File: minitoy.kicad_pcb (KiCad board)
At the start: 2 copper layers, 44 x 40 mm, 37 parts, among them J1 Conn_01x06, J2 PMOD1, J4 USB_B_Micro, J5 PMOD2, U1 ICE40UP5K-SG48, U2 ESP-12E, U3 MIC5504-3.3YM5, U4 MIC5504-1.2YM5, U5 MIC5504-3.3YM5

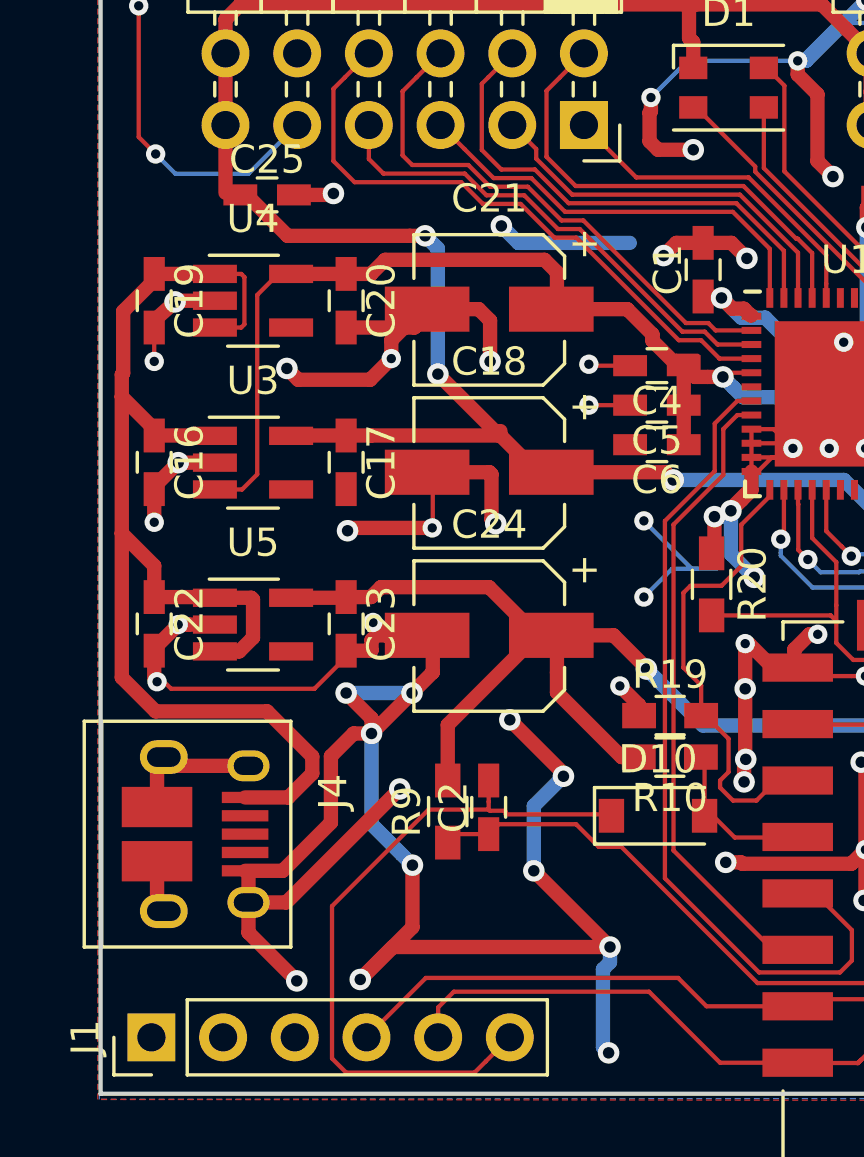
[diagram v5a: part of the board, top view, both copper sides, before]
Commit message: Fix 3d models, change USB footprint
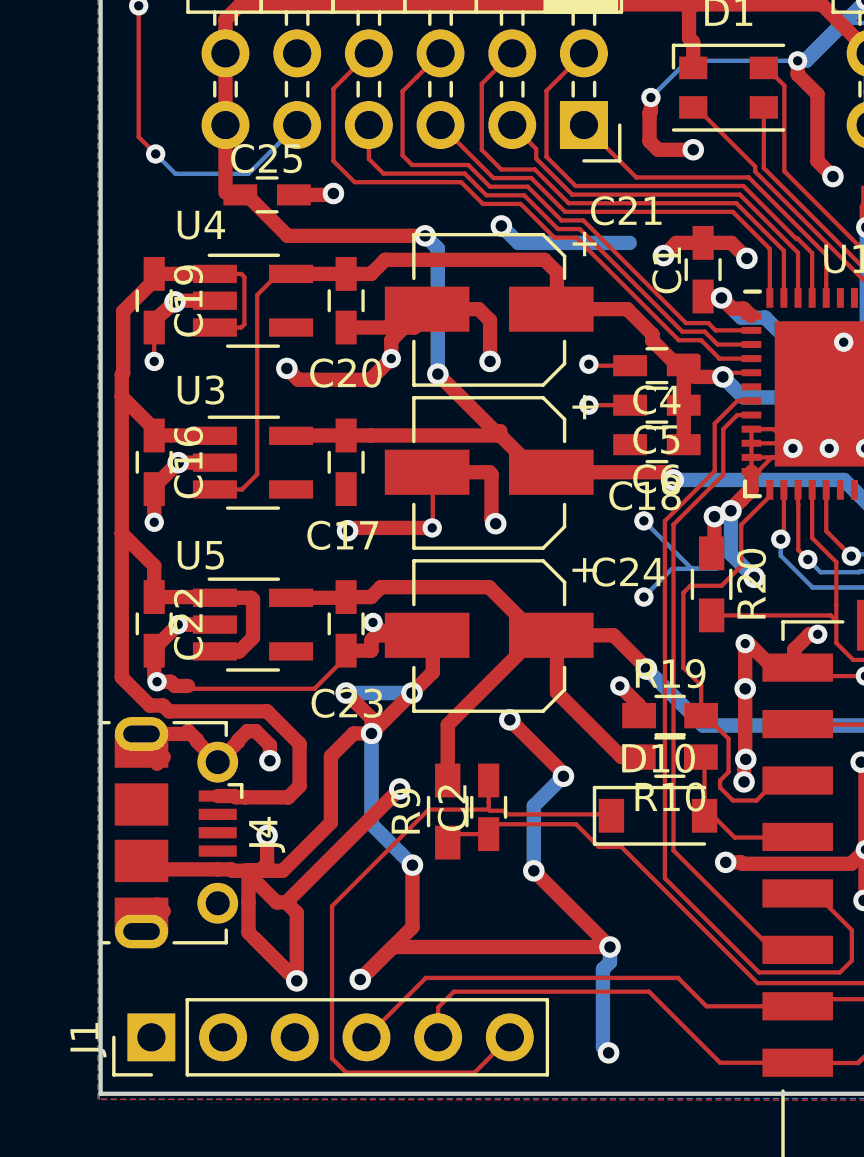
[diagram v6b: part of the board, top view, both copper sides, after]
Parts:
- J4: footprint Connectors:USB_Micro-B_10103594-0001LF -> Connectors_USB:USB_Micro-B_Molex-105017-0001
- moved J4 1.82 mm to (92.8, 130.8)
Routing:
- net GND: track 354.0 -> 367.6 mm, vias 88 -> 90
- net VDD: track 45.2 -> 45.8 mm

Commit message: Finish silk, fix USB cutout for OSH Park, finalize design
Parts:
- added REF**: KiCAD Logo, Symbols:Symbol_KiCAD-Logo_CopperAndSilkScreenTop, F.Cu at (131.9, 116.8)
- added REF***: OSHW-Logo_5.7x6mm_SilkScreen, Symbols:OSHW-Logo_5.7x6mm_SilkScreen, F.Cu at (110.6, 135.9)
- C1, C10, C11, C12, C13, C14, C16, C17, C19, C2, C20, C22, C23, C25, C3, C4, C5, C6: footprint Capacitors_SMD:C_0603_HandSoldering -> Capacitors_SMD:C_0603
- R10, R14, R19, R20, R9: footprint Resistors_SMD:R_0603_HandSoldering -> Resistors_SMD:R_0603
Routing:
- net GND: track 367.6 -> 405.1 mm, vias 90 -> 94
- net FPGA_CRESET: track 22.6 -> 23.4 mm
- net +3.3VA: track 48.4 -> 49.1 mm
- net +1V2: track 46.7 -> 46.1 mm
- net Net-(C2-Pad1): track 30.7 -> 31.3 mm
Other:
- outline, holes or cut-outs redrawn
- board text added: "PMOD1"
- board text added: "PMOD2"
- board text added: "a.litt 2/22/18"
- board text added: "minitoy v0.1"

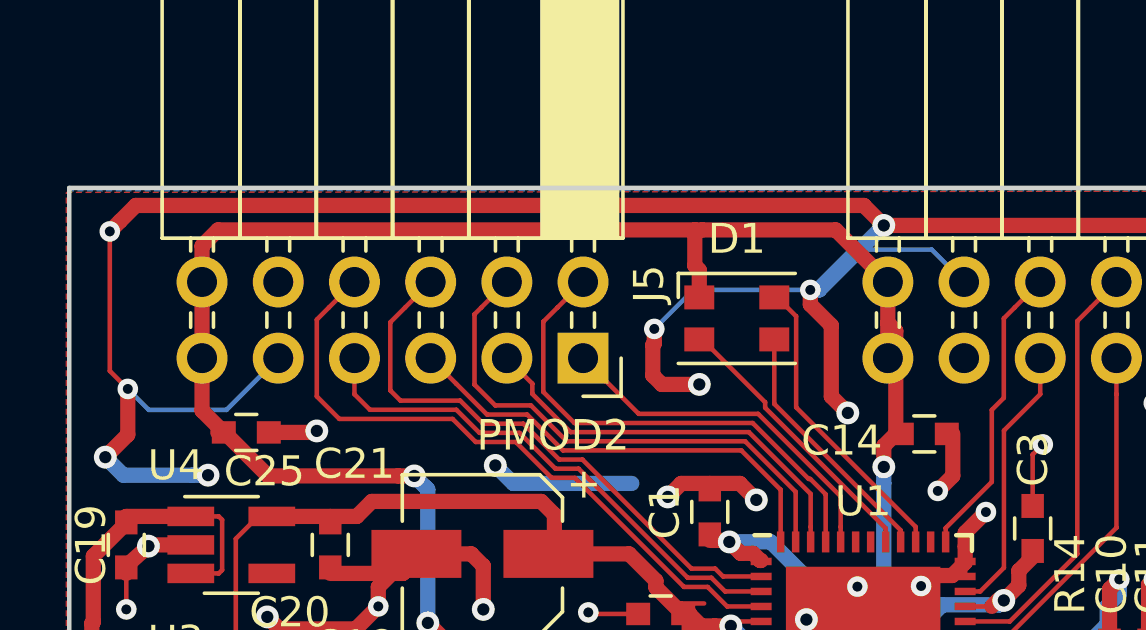
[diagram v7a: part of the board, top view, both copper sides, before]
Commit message: Last minute fix for possible short
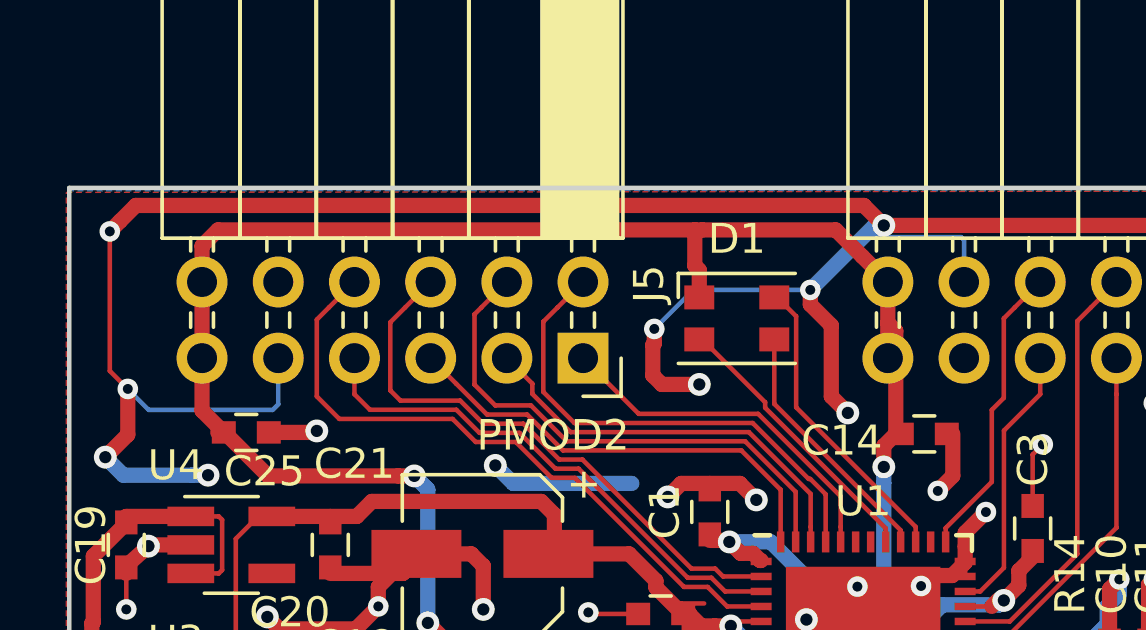
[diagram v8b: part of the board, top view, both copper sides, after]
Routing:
- net GND: track 405.1 -> 407.2 mm
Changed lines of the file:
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@@
     (thickness 1.6)
     (drawings 17)
-    (tracks 912)
+    (tracks 914)
     (zones 0)
     (modules 39)
@@
   (segment (start 122.15 113.75) (end 122.65 113.25) (width 0.508) (layer F.Cu) (net 1))
   (via (at 122.15 113.75) (size 0.762) (drill 0.4064) (layers F.Cu B.Cu) (net 1))
+  (segment (start 97.965 107.215) (end 97.78 107.4) (width 0.1524) (layer B.Cu) (net 2))
+  (segment (start 97.965 105.675) (end 97.965 107.215) (width 0.1524) (layer B.Cu) (net 2))
+  (segment (start 97.78 107.4) (end 93.65 107.4) (width 0.1524) (layer B.Cu) (net 2))
+  (segment (start 93.65 107.4) (end 92.95 106.7) (width 0.1524) (layer B.Cu) (net 2))
+  (segment (start 120.825 101.735) (end 120.73 101.64) (width 0.1524) (layer B.Cu) (net 2))
+  (segment (start 120.825 103.135) (end 120.825 101.735) (width 0.1524) (layer B.Cu) (net 2))
+  (segment (start 120.73 101.64) (end 117.46 101.64) (width 0.1524) (layer B.Cu) (net 2))
+  (segment (start 117.46 101.64) (end 115.7 103.4) (width 0.1524) (layer B.Cu) (net 2))
+  (segment (start 115.7 103.4) (end 117.85 101.25) (width 0.508) (layer B.Cu) (net 2))
+  (segment (start 117.85 101.25) (end 118.15 101.25) (width 0.508) (layer B.Cu) (net 2))
   (segment (start 92.45 131.75) (end 92.45 133.008) (width 0.508) (layer F.Cu) (net 2))
   (segment (start 92.45 133.008) (end 92.45 133.43699) (width 0.508) (layer F.Cu) (net 2))
@@
   (segment (start 118.15 101.25) (end 133.75 101.25) (width 0.508) (layer F.Cu) (net 2))
   (via (at 133.75 101.25) (size 0.762) (drill 0.4064) (layers F.Cu B.Cu) (net 2))
-  (segment (start 116 103.4) (end 118.15 101.25) (width 0.508) (layer B.Cu) (net 2))
-  (segment (start 115.7 103.4) (end 116 103.4) (width 0.508) (layer B.Cu) (net 2))
   (via (at 118.15 101.25) (size 0.762) (drill 0.4064) (layers F.Cu B.Cu) (net 2))
   (segment (start 116.4 106.95) (end 116.95 107.5) (width 0.508) (layer F.Cu) (net 2))
@@
   (segment (start 115.7 103.4) (end 111.8 103.4) (width 0.1524) (layer B.Cu) (net 2))
   (via (at 110.5 104.7) (size 0.6858) (drill 0.3302) (layers F.Cu B.Cu) (net 2))
-  (segment (start 119.746399 102.056399) (end 117.043601 102.056399) (width 0.1524) (layer B.Cu) (net 2))
-  (segment (start 120.825 103.135) (end 119.746399 102.056399) (width 0.1524) (layer B.Cu) (net 2))
-  (segment (start 117.043601 102.056399) (end 115.7 103.4) (width 0.1524) (layer B.Cu) (net 2))
   (via (at 115.7 103.4) (size 0.6858) (drill 0.3302) (layers F.Cu B.Cu) (net 2))
   (segment (start 92.35 106.1) (end 92.35 101.45) (width 0.1524) (layer F.Cu) (net 2))
   (segment (start 92.95 106.7) (end 92.35 106.1) (width 0.1524) (layer F.Cu) (net 2))
   (via (at 92.35 101.45) (size 0.6858) (drill 0.3302) (layers F.Cu B.Cu) (net 2))
-  (segment (start 96.24 107.4) (end 93.65 107.4) (width 0.1524) (layer B.Cu) (net 2))
-  (segment (start 97.965 105.675) (end 96.24 107.4) (width 0.1524) (layer B.Cu) (net 2))
-  (segment (start 93.65 107.4) (end 92.95 106.7) (width 0.1524) (layer B.Cu) (net 2))
   (via (at 92.95 106.7) (size 0.6858) (drill 0.3302) (layers F.Cu B.Cu) (net 2))
   (segment (start 108.351 114.201) (end 108.3 114.15) (width 0.1524) (layer F.Cu) (net 2))
